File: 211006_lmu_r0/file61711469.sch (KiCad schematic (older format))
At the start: 5 parts

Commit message: Updated BOM and footprints for non-hv components
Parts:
- gave numbers to parts that had none: 5
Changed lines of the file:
@@
 $EndDescr
 $Comp
-L SamacSys_Parts:ADS7038QRTERQ1 IC?
+L SamacSys_Parts:ADS7038QRTERQ1 IC1
 U 1 1 616C53F1
 P 6200 3550
-F 0 "IC?" H 6400 2700 50  0000 L CNN
+F 0 "IC1" H 6400 2700 50  0000 L CNN
 F 1 "ADS7038QRTERQ1" H 6400 2600 50  0000 L CNN
 F 2 "QFN50P300X300X80-17N-D" H 7450 4250 50  0001 L CNN
@@
 	3700 5100 3400 5100
 $Comp
-L Device:Ferrite_Bead_Small FB?
+L Device:Ferrite_Bead_Small FB1
 U 1 1 616D49CF
 P 7700 3450
-F 0 "FB?" V 7450 3550 50  0000 C CNN
+F 0 "FB1" V 7450 3550 50  0000 C CNN
 F 1 "Ferrite_Bead_Small" V 7550 3850 50  0000 C CNN
 F 2 "" V 7630 3450 50  0001 C CNN
@@
 $EndComp
 $Comp
-L Device:C C?
+L Device:C C15
 U 1 1 616D6459
 P 8450 3600
-F 0 "C?" H 8565 3646 50  0000 L CNN
+F 0 "C15" H 8565 3646 50  0000 L CNN
 F 1 "C" H 8565 3555 50  0000 L CNN
 F 2 "" H 8488 3450 50  0001 C CNN
@@
 	8450 3450 8450 3350
 $Comp
-L Device:C C?
+L Device:C C16
 U 1 1 616F1E82
 P 8750 3600
-F 0 "C?" H 8865 3646 50  0000 L CNN
+F 0 "C16" H 8865 3646 50  0000 L CNN
 F 1 "C" H 8865 3555 50  0000 L CNN
 F 2 "" H 8788 3450 50  0001 C CNN
@@
 	7800 3450 8150 3450
 $Comp
-L Device:C C?
+L Device:C C14
 U 1 1 616D6F8A
 P 8150 3600
-F 0 "C?" H 8265 3646 50  0000 L CNN
+F 0 "C14" H 8265 3646 50  0000 L CNN
 F 1 "C" H 8265 3555 50  0000 L CNN
 F 2 "" H 8188 3450 50  0001 C CNN

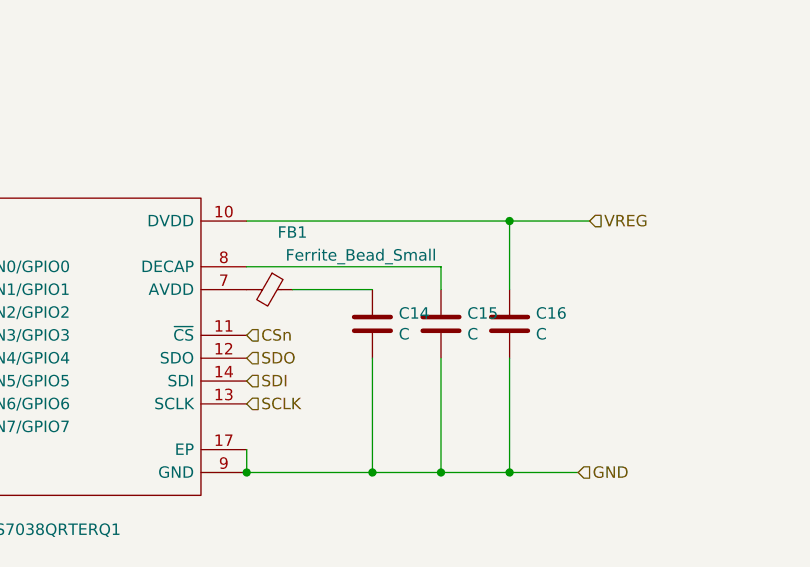
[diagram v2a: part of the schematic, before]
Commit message: Added most footprint requirements in HV
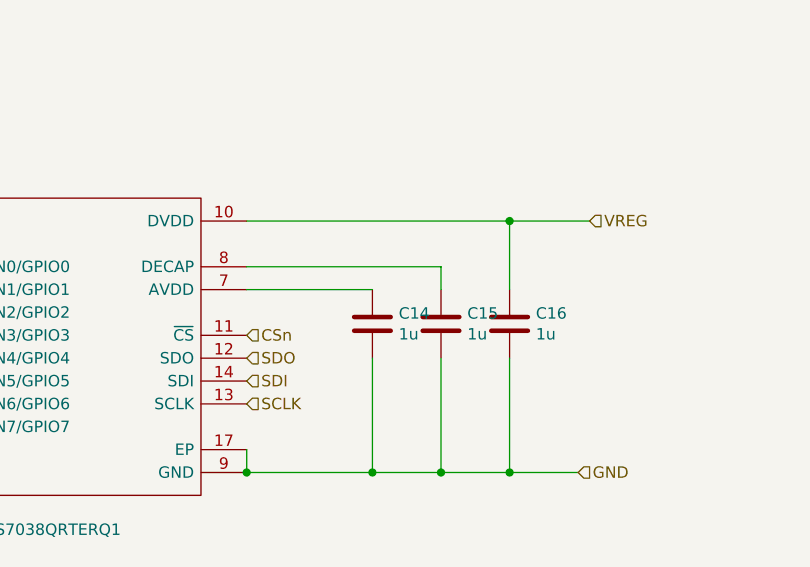
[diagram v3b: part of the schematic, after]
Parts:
- removed FB1: Ferrite_Bead_Small, symbol Device:Ferrite_Bead_Small
- C14, C15, C16: value C -> 1u; footprint (none) -> Capacitor_SMD:C_0603_1608Metric_Pad1.08x0.95mm_HandSolder
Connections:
- net at IC1.7 (AVDD): now also C14.1
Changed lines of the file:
@@
 Wire Wire Line
 	3700 5100 3400 5100
-$Comp
-L Device:Ferrite_Bead_Small FB1
-U 1 1 616D49CF
-P 7700 3450
-F 0 "FB1" V 7450 3550 50  0000 C CNN
-F 1 "Ferrite_Bead_Small" V 7550 3850 50  0000 C CNN
-F 2 "" V 7630 3450 50  0001 C CNN
-F 3 "~" H 7700 3450 50  0001 C CNN
-	1    7700 3450
-	0    1    1    0
-$EndComp
-$Comp
-L Device:C C15
-U 1 1 616D6459
-P 8450 3600
-F 0 "C15" H 8565 3646 50  0000 L CNN
-F 1 "C" H 8565 3555 50  0000 L CNN
-F 2 "" H 8488 3450 50  0001 C CNN
-F 3 "~" H 8450 3600 50  0001 C CNN
-	1    8450 3600
-	1    0    0    -1
-$EndComp
 Wire Wire Line
 	8450 3350 7600 3350
@@
 Wire Wire Line
 	8450 3450 8450 3350
-$Comp
-L Device:C C16
-U 1 1 616F1E82
-P 8750 3600
-F 0 "C16" H 8865 3646 50  0000 L CNN
-F 1 "C" H 8865 3555 50  0000 L CNN
-F 2 "" H 8788 3450 50  0001 C CNN
-F 3 "~" H 8750 3600 50  0001 C CNN
-	1    8750 3600
-	1    0    0    -1
-$EndComp
 Wire Wire Line
 	8750 3750 8750 4250
@@
 Wire Wire Line
 	8150 3750 8150 4250
-Wire Wire Line
-	7800 3450 8150 3450
 $Comp
 L Device:C C14
@@
 P 8150 3600
 F 0 "C14" H 8265 3646 50  0000 L CNN
-F 1 "C" H 8265 3555 50  0000 L CNN
-F 2 "" H 8188 3450 50  0001 C CNN
+F 1 "1u" H 8265 3555 50  0000 L CNN
+F 2 "Capacitor_SMD:C_0603_1608Metric_Pad1.08x0.95mm_HandSolder" H 8188 3450 50  0001 C CNN
 F 3 "~" H 8150 3600 50  0001 C CNN
 	1    8150 3600
@@
 	9050 4250 8750 4250
 Connection ~ 8750 4250
+Wire Wire Line
+	7600 3450 8150 3450
+$Comp
+L Device:C C15
+U 1 1 61F706A2
+P 8450 3600
+F 0 "C15" H 8565 3646 50  0000 L CNN
+F 1 "1u" H 8565 3555 50  0000 L CNN
+F 2 "Capacitor_SMD:C_0603_1608Metric_Pad1.08x0.95mm_HandSolder" H 8488 3450 50  0001 C CNN
+F 3 "~" H 8450 3600 50  0001 C CNN
+	1    8450 3600
+	1    0    0    -1
+$EndComp
+$Comp
+L Device:C C16
+U 1 1 61F708BB
+P 8750 3600
+F 0 "C16" H 8865 3646 50  0000 L CNN
+F 1 "1u" H 8865 3555 50  0000 L CNN
+F 2 "Capacitor_SMD:C_0603_1608Metric_Pad1.08x0.95mm_HandSolder" H 8788 3450 50  0001 C CNN
+F 3 "~" H 8750 3600 50  0001 C CNN
+	1    8750 3600
+	1    0    0    -1
+$EndComp
 $EndSCHEMATC

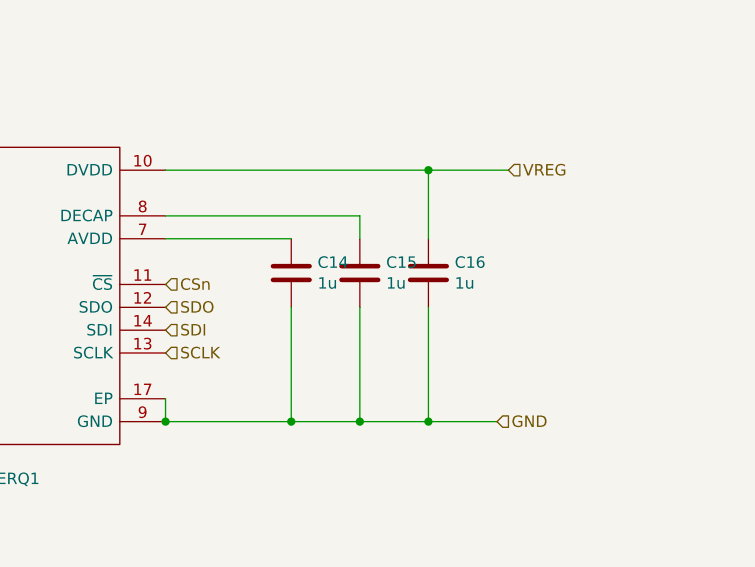
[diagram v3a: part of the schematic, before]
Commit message: Updated with Mouser links for BOM
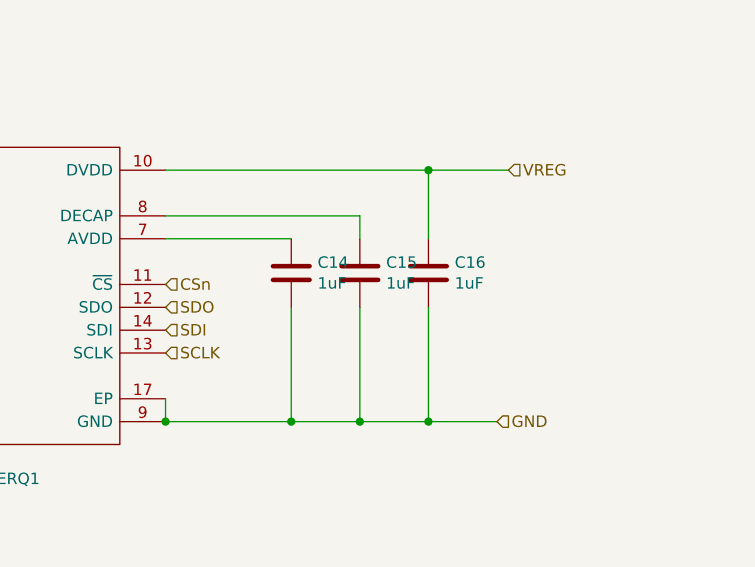
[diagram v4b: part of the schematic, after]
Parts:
- C14, C15, C16: value 1u -> 1uF
- IC1: Manufacturer (none) -> Texas Instruments; Manufacturer_Name Texas Instruments -> (none); Manufacturer_Part_Number ADS7038QRTERQ1 -> (none); Mouser Part Number 595-ADS7038QRTERQ1 -> NOT AVAILABLE!; Mouser URL (none) -> NOT AVAILABLE!; Part Number (none) -> ADS7038QRTERQ1
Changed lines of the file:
@@
 F 4 "ADS7038 Q1 Small 8 Channel 12 Bit ADC With SPI Interface and CRC" H 7450 4050 50  0001 L CNN "Description"
 F 5 "0.8" H 7450 3950 50  0001 L CNN "Height"
-F 6 "595-ADS7038QRTERQ1" H 7450 3850 50  0001 L CNN "Mouser Part Number"
+F 6 "NOT AVAILABLE!" H 7450 3850 50  0001 L CNN "Mouser Part Number"
 F 7 "https://www.mouser.co.uk/ProductDetail/Texas-Instruments/ADS7038QRTERQ1?qs=81r%252BiQLm7BTk46c4kXEtDw%3D%3D" H 7450 3750 50  0001 L CNN "Mouser Price/Stock"
-F 8 "Texas Instruments" H 7450 3650 50  0001 L CNN "Manufacturer_Name"
-F 9 "ADS7038QRTERQ1" H 7450 3550 50  0001 L CNN "Manufacturer_Part_Number"
+F 8 "" H 7450 3650 50  0001 L CNN "Manufacturer_Name"
+F 9 "" H 7450 3550 50  0001 L CNN "Manufacturer_Part_Number"
+F 10 "Texas Instruments" H 6200 3550 50  0001 C CNN "Manufacturer"
+F 11 "ADS7038QRTERQ1" H 6200 3550 50  0001 C CNN "Part Number"
+F 12 "NOT AVAILABLE!" H 6200 3550 50  0001 C CNN "Mouser URL"
 	1    6200 3550
 	1    0    0    -1
@@
 P 8150 3600
 F 0 "C14" H 8265 3646 50  0000 L CNN
-F 1 "1u" H 8265 3555 50  0000 L CNN
+F 1 "1uF" H 8265 3555 50  0000 L CNN
 F 2 "Capacitor_SMD:C_0603_1608Metric_Pad1.08x0.95mm_HandSolder" H 8188 3450 50  0001 C CNN
 F 3 "~" H 8150 3600 50  0001 C CNN
@@
 P 8450 3600
 F 0 "C15" H 8565 3646 50  0000 L CNN
-F 1 "1u" H 8565 3555 50  0000 L CNN
+F 1 "1uF" H 8565 3555 50  0000 L CNN
 F 2 "Capacitor_SMD:C_0603_1608Metric_Pad1.08x0.95mm_HandSolder" H 8488 3450 50  0001 C CNN
 F 3 "~" H 8450 3600 50  0001 C CNN
@@
 P 8750 3600
 F 0 "C16" H 8865 3646 50  0000 L CNN
-F 1 "1u" H 8865 3555 50  0000 L CNN
+F 1 "1uF" H 8865 3555 50  0000 L CNN
 F 2 "Capacitor_SMD:C_0603_1608Metric_Pad1.08x0.95mm_HandSolder" H 8788 3450 50  0001 C CNN
 F 3 "~" H 8750 3600 50  0001 C CNN
